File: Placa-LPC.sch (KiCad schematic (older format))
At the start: 13 parts, among them X1 12MHz

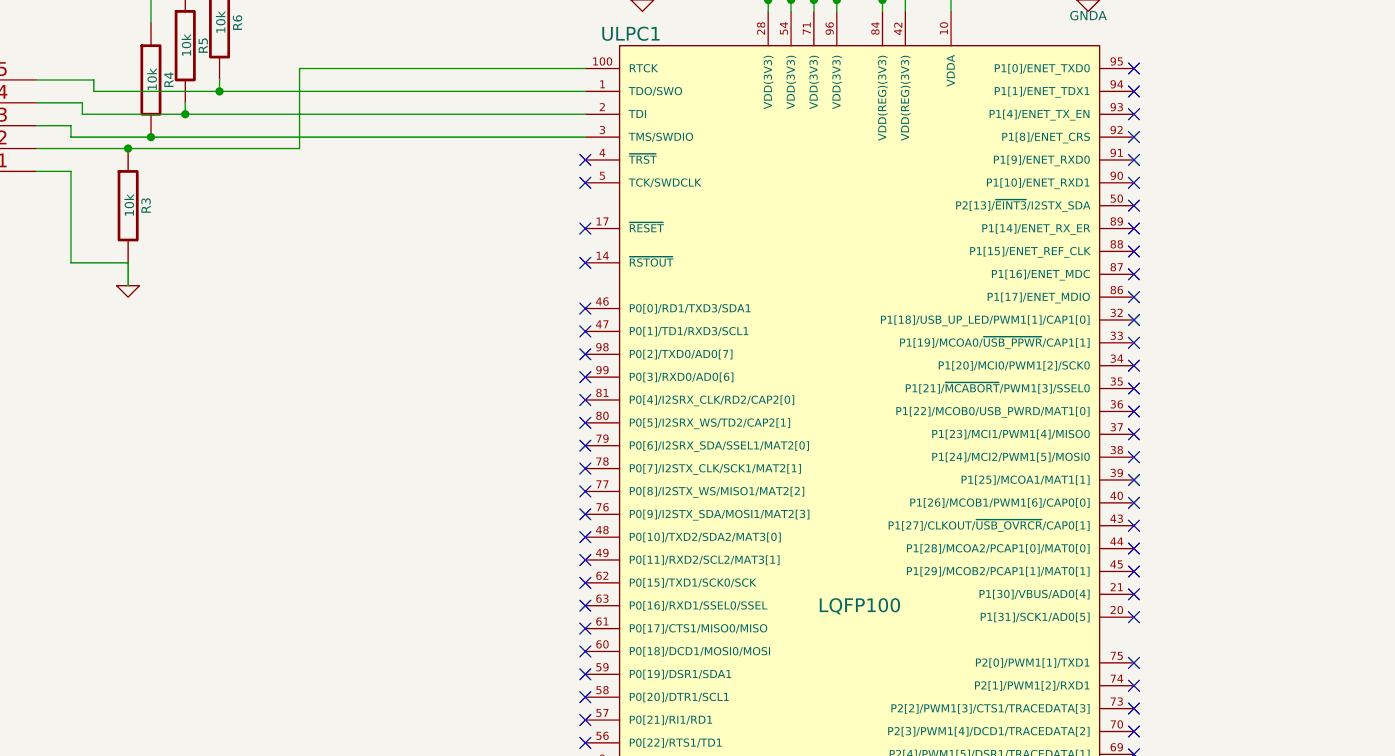
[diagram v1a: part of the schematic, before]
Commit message: Definicion de pines
Definicion de algunos pines y ruteado de algunas pistas.
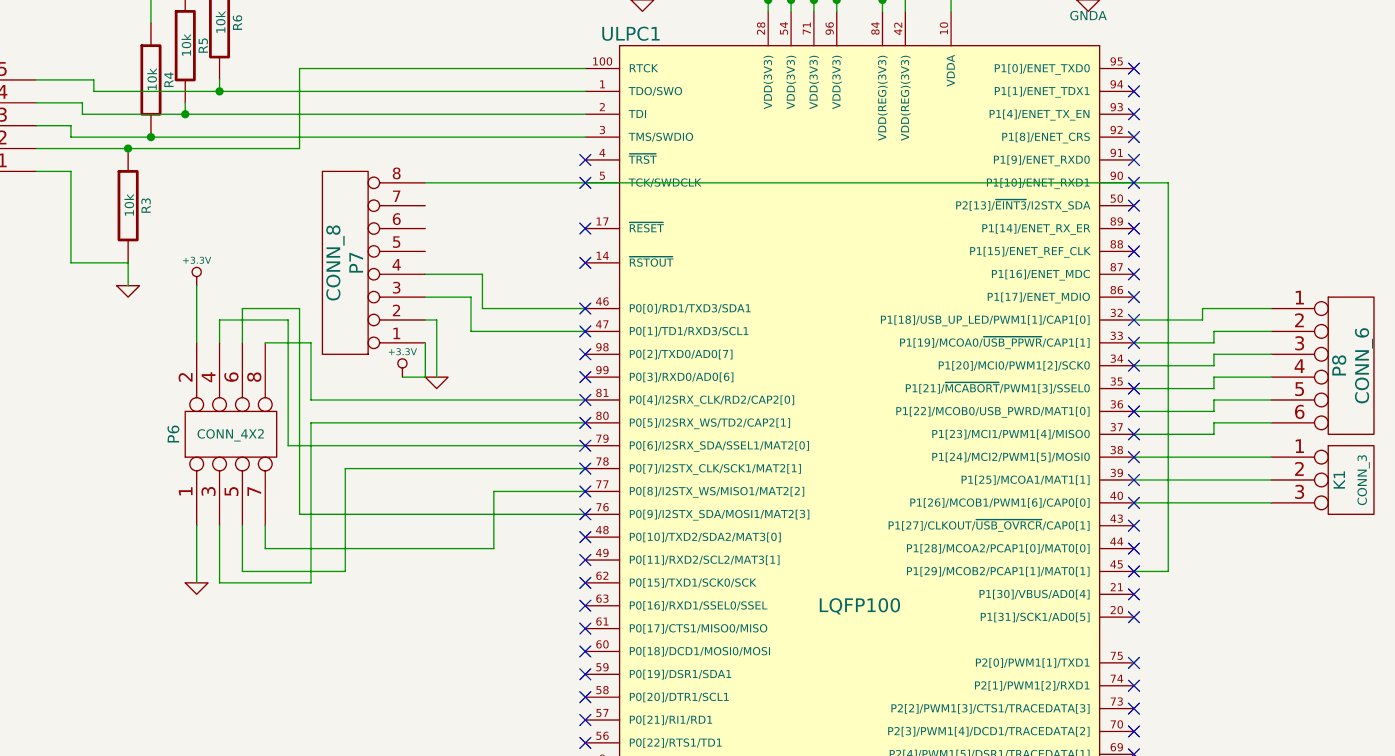
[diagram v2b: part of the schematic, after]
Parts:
- added K1: CONN_3, symbol CONN_3
- added P6: CONN_4X2, symbol CONN_4X2
- added P7: CONN_8, symbol CONN_8
- added P8: CONN_6, symbol CONN_6
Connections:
- net +3.3V: now also P6.2, P7.1 (P1)
- net GND: now also P6.1, P7.2 (P2)
- net at ULPC1.32 (P1[18]/USB_UP_LED/PWM1[1]/CAP1[0]): now also P8.1
- net at ULPC1.33 (P1[19]/MCOA0/~USB_PPWR~/CAP1[1]): now also P8.2
- net at ULPC1.34 (P1[20]/MCI0/PWM1[2]/SCK0): now also P8.3
- net at ULPC1.35 (P1[21]/~MCABORT~/PWM1[3]/SSEL0): now also P8.4
- net at ULPC1.36 (P1[22]/MCOB0/USB_PWRD/MAT1[0]): now also P8.5
- net at ULPC1.37 (P1[23]/MCI1/PWM1[4]/MISO0): now also P8.6
- net at ULPC1.38 (P1[24]/MCI2/PWM1[5]/MOSI0): now also K1.1 (P1)
- net at ULPC1.39 (P1[25]/MCOA1/MAT1[1]): now also K1.2 (PM)
- net at ULPC1.40 (P1[26]/MCOB1/PWM1[6]/CAP0[0]): now also K1.3 (P3)
- net at ULPC1.45 (P1[29]/MCOB2/PCAP1[1]/MAT0[1]): now also P7.8 (P8)
- net at ULPC1.46 (P0[0]/RD1/TXD3/SDA1): now also P7.4 (P4)
- net at ULPC1.47 (P0[1]/TD1/RXD3/SCL1): now also P7.3 (P3)
- net at ULPC1.76 (P0[9]/I2STX_SDA/MOSI1/MAT2[3]): now also P6.6
- net at ULPC1.77 (P0[8]/I2STX_WS/MISO1/MAT2[2]): now also P6.7
- net at ULPC1.78 (P0[7]/I2STX_CLK/SCK1/MAT2[1]): now also P6.5
- net at ULPC1.79 (P0[6]/I2SRX_SDA/SSEL1/MAT2[0]): now also P6.4
- net at ULPC1.80 (P0[5]/I2SRX_WS/TD2/CAP2[1]): now also P6.3
- net at ULPC1.81 (P0[4]/I2SRX_CLK/RD2/CAP2[0]): now also P6.8

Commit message: Actualizado desde mi pc
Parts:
- added K2: CONN_3, symbol CONN_3
- added P9: CONN_6, symbol CONN_6
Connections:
- net at ULPC1.24 (P0[28]/SCL0/USB_SCL): now also P8.1
- net at ULPC1.25 (P0[27]/SDA0/USB_SDA): now also P8.2
- net at ULPC1.26 (P3[26]/STCLK/MAT0[1]/PWM1[3]): now also P8.3
- net at ULPC1.27 (P3[25]/MAT0[0]/PWM1[2]): now also P8.4
- net at ULPC1.29 (P0[29]/USB_D+): now also P8.5
- net at ULPC1.30 (P0[30]/USB_D-): now also P8.6
- net at ULPC1.32 (P1[18]/USB_UP_LED/PWM1[1]/CAP1[0]): now also K1.1 (P1); no longer P8.1
- net at ULPC1.33 (P1[19]/MCOA0/~USB_PPWR~/CAP1[1]): now also K1.2 (PM); no longer P8.2
- net at ULPC1.34 (P1[20]/MCI0/PWM1[2]/SCK0): now also K1.3 (P3); no longer P8.3
- net at ULPC1.35 (P1[21]/~MCABORT~/PWM1[3]/SSEL0): now also K2.3 (P3); no longer P8.4
- net at ULPC1.36 (P1[22]/MCOB0/USB_PWRD/MAT1[0]): now also K2.2 (PM); no longer P8.5
- net at ULPC1.37 (P1[23]/MCI1/PWM1[4]/MISO0): now also K2.1 (P1); no longer P8.6
- net at ULPC1.38 (P1[24]/MCI2/PWM1[5]/MOSI0): now also P9.6; no longer K1.1 (P1)
- net at ULPC1.39 (P1[25]/MCOA1/MAT1[1]): now also P9.5; no longer K1.2 (PM)
- net at ULPC1.40 (P1[26]/MCOB1/PWM1[6]/CAP0[0]): now also P9.4; no longer K1.3 (P3)
- net at ULPC1.43 (P1[27]/CLKOUT/~USB_OVRCR~/CAP0[1]): now also P9.3
- net at ULPC1.44 (P1[28]/MCOA2/PCAP1[0]/MAT0[0]): now also P9.2
- net at ULPC1.48 (P0[10]/TXD2/SDA2/MAT3[0]): now also P9.1
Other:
- moved on the sheet: K1, P8
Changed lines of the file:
@@
 Sheet 1 2
 Title ""
-Date "19 oct 2015"
+Date "20 oct 2015"
 Rev ""
 Comp ""
@@
 	6500 2700 6250 2700
 Wire Wire Line
-	6250 2300 9500 2300
+	6250 2300 6850 2300
 $Comp
 L CONN_6 P8
 U 1 1 56244F3D
-P 10300 3100
-F 0 "P8" V 10250 3100 60  0000 C CNN
-F 1 "CONN_6" V 10350 3100 60  0000 C CNN
-F 2 "" H 10300 3100 60  0000 C CNN
-F 3 "" H 10300 3100 60  0000 C CNN
-	1    10300 3100
-	1    0    0    -1
+P 5450 5250
+F 0 "P8" V 5400 5250 60  0000 C CNN
+F 1 "CONN_6" V 5500 5250 60  0000 C CNN
+F 2 "" H 5450 5250 60  0000 C CNN
+F 3 "" H 5450 5250 60  0000 C CNN
+	1    5450 5250
+	-1   0    0    1
 $EndComp
 $Comp
 L CONN_3 K1
 U 1 1 56244F4C
-P 10300 3600
-F 0 "K1" V 10250 3600 50  0000 C CNN
-F 1 "CONN_3" V 10350 3600 40  0000 C CNN
-F 2 "" H 10300 3600 60  0000 C CNN
-F 3 "" H 10300 3600 60  0000 C CNN
-	1    10300 3600
-	1    0    0    -1
-$EndComp
-Wire Wire Line
-	9350 2900 9650 2900
-Wire Wire Line
-	9650 2900 9650 2850
-Wire Wire Line
-	9650 2850 9950 2850
-Wire Wire Line
-	9950 2950 9700 2950
-Wire Wire Line
-	9700 2950 9700 3000
-Wire Wire Line
-	9700 3000 9350 3000
-Wire Wire Line
-	9350 3100 9700 3100
-Wire Wire Line
-	9700 3100 9700 3050
-Wire Wire Line
-	9700 3050 9950 3050
-Wire Wire Line
-	9350 3200 9700 3200
-Wire Wire Line
-	9700 3200 9700 3150
-Wire Wire Line
-	9700 3150 9950 3150
-Wire Wire Line
-	9350 3300 9700 3300
-Wire Wire Line
-	9700 3300 9700 3250
-Wire Wire Line
-	9700 3250 9950 3250
-Wire Wire Line
-	9350 3400 9700 3400
-Wire Wire Line
-	9700 3400 9700 3350
-Wire Wire Line
-	9700 3350 9950 3350
-Wire Wire Line
-	9350 3500 9950 3500
-Wire Wire Line
-	9350 3600 9950 3600
-Wire Wire Line
-	9350 3700 9950 3700
-Wire Wire Line
-	9500 2300 9500 4000
+P 10300 2950
+F 0 "K1" V 10250 2950 50  0000 C CNN
+F 1 "CONN_3" V 10350 2950 40  0000 C CNN
+F 2 "" H 10300 2950 60  0000 C CNN
+F 3 "" H 10300 2950 60  0000 C CNN
+	1    10300 2950
+	1    0    0    -1
+$EndComp
+Wire Wire Line
+	9500 2350 9500 4000
 Wire Wire Line
 	9500 4000 9350 4000
+$Comp
+L CONN_6 P9
+U 1 1 56269EC2
+P 5450 4600
+F 0 "P9" V 5400 4600 60  0000 C CNN
+F 1 "CONN_6" V 5500 4600 60  0000 C CNN
+F 2 "" H 5450 4600 60  0000 C CNN
+F 3 "" H 5450 4600 60  0000 C CNN
+	1    5450 4600
+	-1   0    0    1
+$EndComp
+$Comp
+L CONN_3 K2
+U 1 1 56269F4B
+P 10300 3300
+F 0 "K2" V 10250 3300 50  0000 C CNN
+F 1 "CONN_3" V 10350 3300 40  0000 C CNN
+F 2 "" H 10300 3300 60  0000 C CNN
+F 3 "" H 10300 3300 60  0000 C CNN
+	1    10300 3300
+	1    0    0    -1
+$EndComp
+Wire Wire Line
+	5800 4850 6200 4850
+Wire Wire Line
+	6200 4850 6200 3850
+Wire Wire Line
+	6200 3850 6950 3850
+Wire Wire Line
+	9350 3900 9800 3900
+Wire Wire Line
+	9800 3900 9800 4750
+Wire Wire Line
+	9800 4750 8150 4750
+Wire Wire Line
+	6650 4750 5800 4750
+Wire Wire Line
+	9350 3800 9700 3800
+Wire Wire Line
+	9700 3800 9700 4650
+Wire Wire Line
+	9700 4650 8150 4650
+Wire Wire Line
+	6650 4650 5800 4650
+Wire Wire Line
+	9350 3700 9650 3700
+Wire Wire Line
+	9650 3700 9650 4550
+Wire Wire Line
+	9650 4550 8150 4550
+Wire Wire Line
+	6650 4550 5800 4550
+Wire Wire Line
+	9350 3600 9600 3600
+Wire Wire Line
+	9600 3600 9600 4450
+Wire Wire Line
+	9600 4450 8150 4450
+Wire Wire Line
+	6650 4450 5800 4450
+Wire Wire Line
+	9350 3500 9550 3500
+Wire Wire Line
+	9550 3500 9550 4350
+Wire Wire Line
+	9550 4350 8150 4350
+Wire Wire Line
+	6650 4350 5800 4350
+Wire Wire Line
+	9350 3400 9650 3400
+Wire Wire Line
+	9650 3400 9650 3200
+Wire Wire Line
+	9650 3200 9950 3200
+Wire Wire Line
+	9350 3300 9950 3300
+Wire Wire Line
+	9350 3200 9600 3200
+Wire Wire Line
+	9600 3200 9600 3350
+Wire Wire Line
+	9600 3350 9800 3350
+Wire Wire Line
+	9800 3350 9800 3400
+Wire Wire Line
+	9800 3400 9950 3400
+Wire Wire Line
+	9350 3100 9950 3100
+Wire Wire Line
+	9950 3100 9950 3050
+Wire Wire Line
+	9950 2950 9950 3000
+Wire Wire Line
+	9950 3000 9350 3000
+Wire Wire Line
+	9350 2900 9950 2900
+Wire Wire Line
+	9950 2900 9950 2850
+Wire Wire Line
+	5800 5000 6700 5000
+Wire Wire Line
+	6700 5000 6700 5550
+Wire Wire Line
+	6700 5550 6950 5550
+Wire Wire Line
+	6950 5450 6650 5450
+Wire Wire Line
+	6650 5450 6650 5100
+Wire Wire Line
+	6650 5100 5800 5100
+Wire Wire Line
+	6950 5250 6550 5250
+Wire Wire Line
+	6550 5250 6550 5400
+Wire Wire Line
+	6550 5400 5800 5400
+Wire Wire Line
+	6950 5350 6600 5350
+Wire Wire Line
+	6600 5350 6600 5500
+Wire Wire Line
+	6600 5500 5800 5500
+Wire Wire Line
+	9350 5800 7350 5800
+Wire Wire Line
+	7350 5800 7350 5650
+Wire Wire Line
+	7350 5650 6400 5650
+Wire Wire Line
+	6400 5650 6400 5200
+Wire Wire Line
+	6400 5200 5800 5200
+Wire Wire Line
+	5800 5300 6350 5300
+Wire Wire Line
+	6350 5300 6350 5700
+Wire Wire Line
+	6350 5700 7300 5700
+Wire Wire Line
+	7300 5700 7300 5900
+Wire Wire Line
+	7300 5900 9350 5900
+Wire Wire Line
+	6650 4350 6650 4300
+Wire Wire Line
+	6650 4300 8150 4300
+Wire Wire Line
+	8150 4300 8150 4350
+Connection ~ 8150 4350
+Connection ~ 6650 4350
+Wire Wire Line
+	6650 4450 6650 4400
+Wire Wire Line
+	6650 4400 8150 4400
+Wire Wire Line
+	8150 4400 8150 4450
+Connection ~ 8150 4450
+Connection ~ 6650 4450
+Wire Wire Line
+	6650 4550 6650 4500
+Wire Wire Line
+	6650 4500 8150 4500
+Wire Wire Line
+	8150 4500 8150 4550
+Connection ~ 8150 4550
+Connection ~ 6650 4550
+Wire Wire Line
+	6650 4650 6650 4600
+Wire Wire Line
+	6650 4600 8150 4600
+Wire Wire Line
+	8150 4600 8150 4650
+Connection ~ 8150 4650
+Connection ~ 6650 4650
+Wire Wire Line
+	8150 4750 8150 4700
+Wire Wire Line
+	8150 4700 6650 4700
+Connection ~ 8150 4750
+Wire Wire Line
+	6650 4700 6650 4750
+Connection ~ 6650 4750
+Wire Wire Line
+	6850 2300 6850 2350
+Wire Wire Line
+	6850 2350 9500 2350
+Connection ~ 9500 2350
+Connection ~ 6800 2300
 $EndSCHEMATC

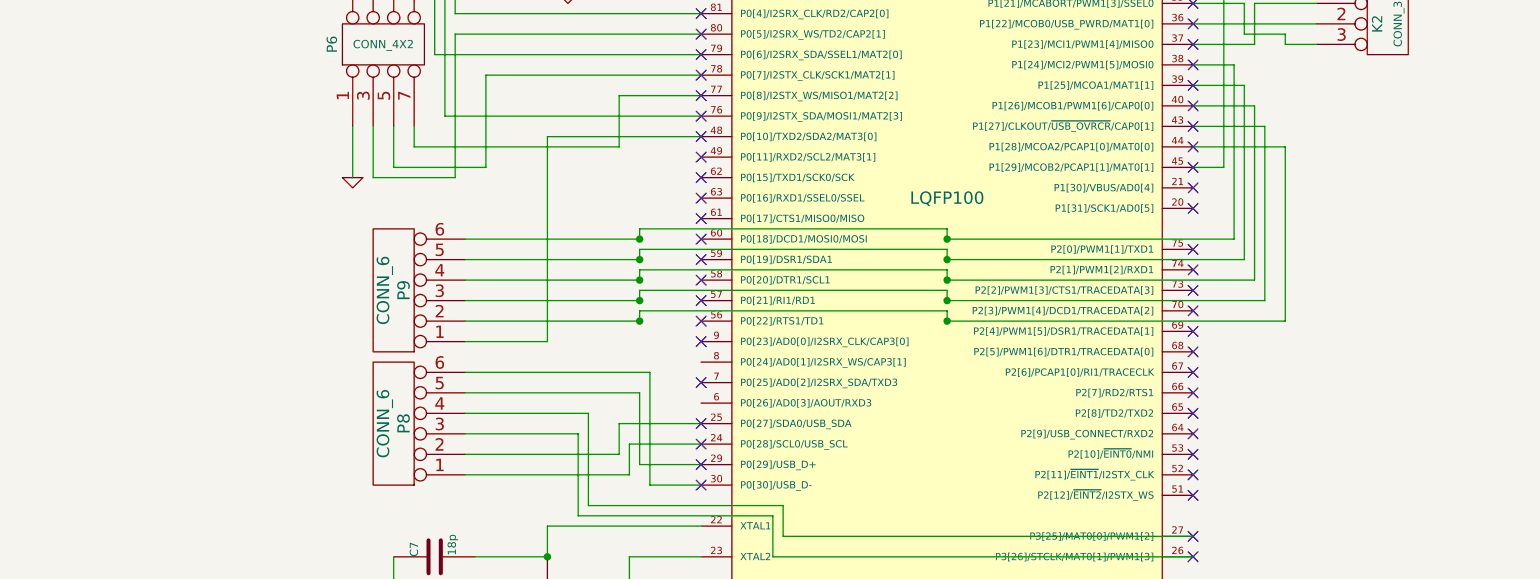
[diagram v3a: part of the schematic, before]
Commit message: Ruteo pines
Ruteo completo de pines motor y módulos.
Falta pines programación y pines adc para batería.
Falta definir conectores.
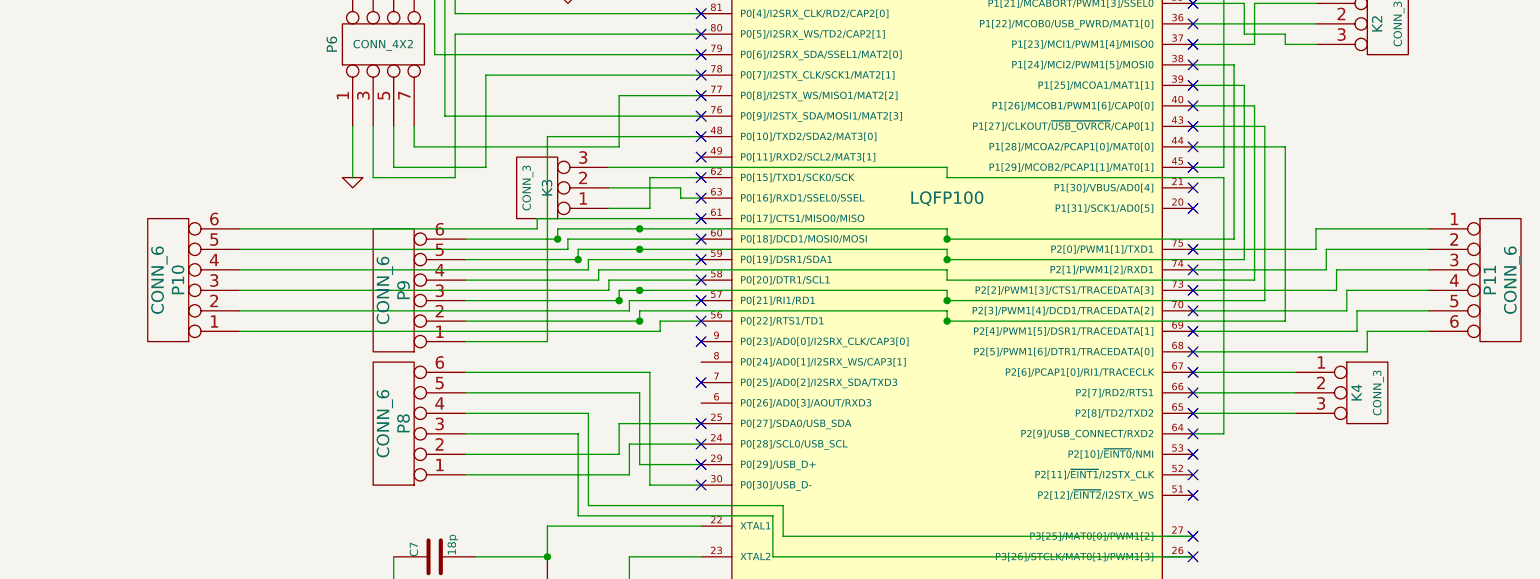
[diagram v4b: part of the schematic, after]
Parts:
- added K3, K4: CONN_3, symbol CONN_3
- added P10, P11: CONN_6, symbol CONN_6
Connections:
- net at ULPC1.56 (P0[22]/RTS1/TD1): now also P10.1
- net at ULPC1.57 (P0[21]/RI1/RD1): now also P10.2
- net at ULPC1.58 (P0[20]/DTR1/SCL1): now also P10.3
- net at ULPC1.59 (P0[19]/DSR1/SDA1): now also P10.4
- net at ULPC1.60 (P0[18]/DCD1/MOSI0/MOSI): now also P10.5
- net at ULPC1.61 (P0[17]/CTS1/MISO0/MISO): now also P10.6
- net at ULPC1.62 (P0[15]/TXD1/SCK0/SCK): now also K3.1 (P1)
- net at ULPC1.63 (P0[16]/RXD1/SSEL0/SSEL): now also K3.2 (PM)
- net at ULPC1.64 (P2[9]/USB_CONNECT/RXD2): now also K3.3 (P3)
- net at ULPC1.65 (P2[8]/TD2/TXD2): now also K4.3 (P3)
- net at ULPC1.66 (P2[7]/RD2/RTS1): now also K4.2 (PM)
- net at ULPC1.67 (P2[6]/PCAP1[0]/RI1/TRACECLK): now also K4.1 (P1)
- net at ULPC1.68 (P2[5]/PWM1[6]/DTR1/TRACEDATA[0]): now also P11.6
- net at ULPC1.69 (P2[4]/PWM1[5]/DSR1/TRACEDATA[1]): now also P11.5
- net at ULPC1.70 (P2[3]/PWM1[4]/DCD1/TRACEDATA[2]): now also P11.4
- net at ULPC1.73 (P2[2]/PWM1[3]/CTS1/TRACEDATA[3]): now also P11.3
- net at ULPC1.74 (P2[1]/PWM1[2]/RXD1): now also P11.2
- net at ULPC1.75 (P2[0]/PWM1[1]/TXD1): now also P11.1
